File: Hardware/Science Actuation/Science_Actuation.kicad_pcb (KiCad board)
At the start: 2 copper layers, 111 parts, among them J4 RJ45_LED_Shielded, Q1 BSS138, Q2 BSS138, Q3 BSS138, Q4 AO3401A, Q5 AO3401A, SW1 SW_Push, SW10 SW_SPDT, SW2 SW_Push, SW3 SW_Push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

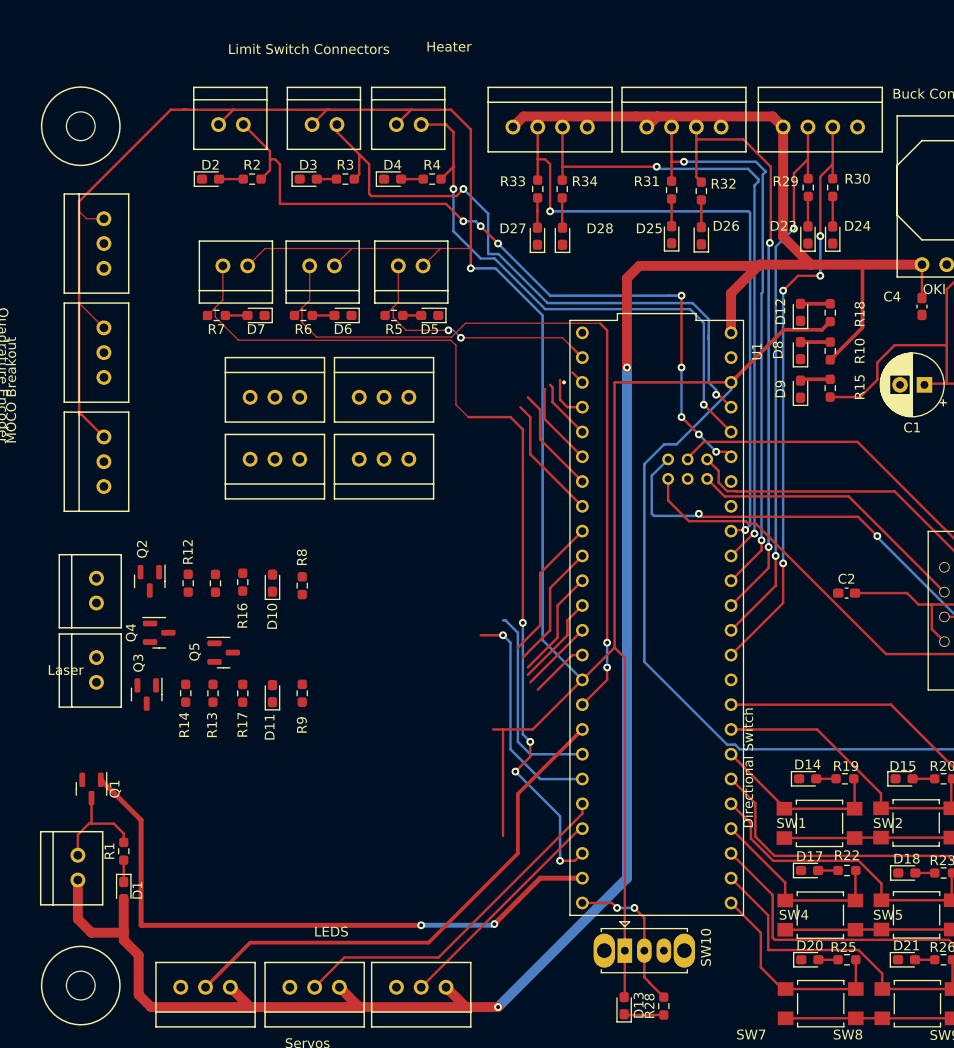
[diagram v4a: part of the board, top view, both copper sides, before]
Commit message: Tried  Cleaning Up Board
Changed layout, added fourth MOCO Breakout
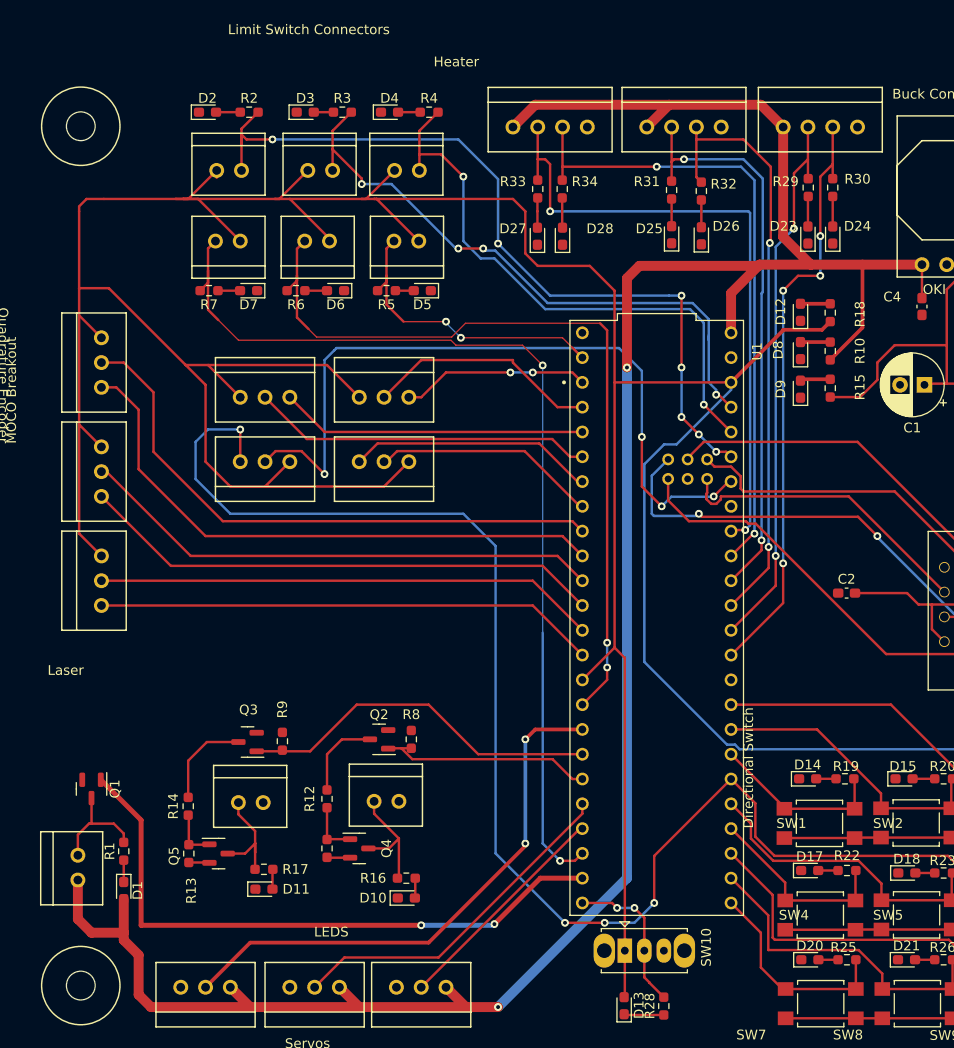
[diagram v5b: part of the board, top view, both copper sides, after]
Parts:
- moved D10 35.1 mm to (49.5, 95.2), turned to 0 degrees
- moved Conn12 35.0 mm to (46.2, 85.3), turned to 0 degrees
- moved R16 34.7 mm to (49.5, 93.2), turned to 180 degrees
- moved Conn16 34.5 mm to (18.3, 65.3)
- moved Q4 30.1 mm to (44.7, 90.2)
- moved R11 29.5 mm to (41.4, 90.2)
- moved Q2 28.5 mm to (46.7, 79.0), turned to 180 degrees
- moved R12 26.3 mm to (41.4, 85.1), turned to 90 degrees
- moved Q5 20.6 mm to (30.3, 90.7)
- moved D11 20.1 mm to (34.9, 94.3), turned to 0 degrees
- moved R8 19.3 mm to (50.0, 79.0), turned to 90 degrees
- moved Conn13 19.1 mm to (32.3, 85.5), turned to 0 degrees
- moved R17 18.2 mm to (34.9, 92.3), turned to 180 degrees
- moved R13 16.6 mm to (27.2, 90.7), turned to 90 degrees
- moved Conn15 12.2 mm to (18.3, 54.1)
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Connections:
- U1 pad 10: Heater_On2 -> Heater_Temp2
- U1 pad 11: Heater_Temp3 -> Heater_On3
- U1 pad 12: Heater_On3 -> Heater_Temp3
- U1 pad 20: MOCO3_FWD -> MOCO4_FWD
- U1 pad 38: MOCO3_RVS -> MOCO4_RVS
- U1 pad 7: Heater_Temp -> Heater_On
- U1 pad 8: Heater_On -> Heater_Temp
- U1 pad 9: Heater_Temp2 -> Heater_On2
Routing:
- net MOCO4_RVS: track 0.00 -> 112.8 mm, vias 0 -> 4
- net MOCO4_FWD: track 0.00 -> 76.1 mm, vias 0 -> 4
- net Heater_On: track 12.9 -> 60.0 mm
- net Heater_On3: track 6.04 -> 51.4 mm
- net Heater_Temp: track 14.7 -> 60.0 mm
- net Heater_On2: track 9.43 -> 53.9 mm
- net Heater_Temp3: track 7.54 -> 51.4 mm
- net Heater_Temp2: track 11.2 -> 53.9 mm
- net +3V3: track 482.4 -> 510.1 mm, vias 2 -> 1
- net MOCO2_FWD: track 8.62 -> 35.0 mm
- net MOCO2_RVS: track 6.21 -> 31.4 mm
- net MOCO3_FWD: track 4.63 -> 24.1 mm
- net MOCO3_RVS: track 1.44 -> 19.3 mm, vias 0 -> 2
- net Pump2: track 20.4 -> 37.6 mm
- net MOCO1_RVS: track 11.0 -> 25.3 mm
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
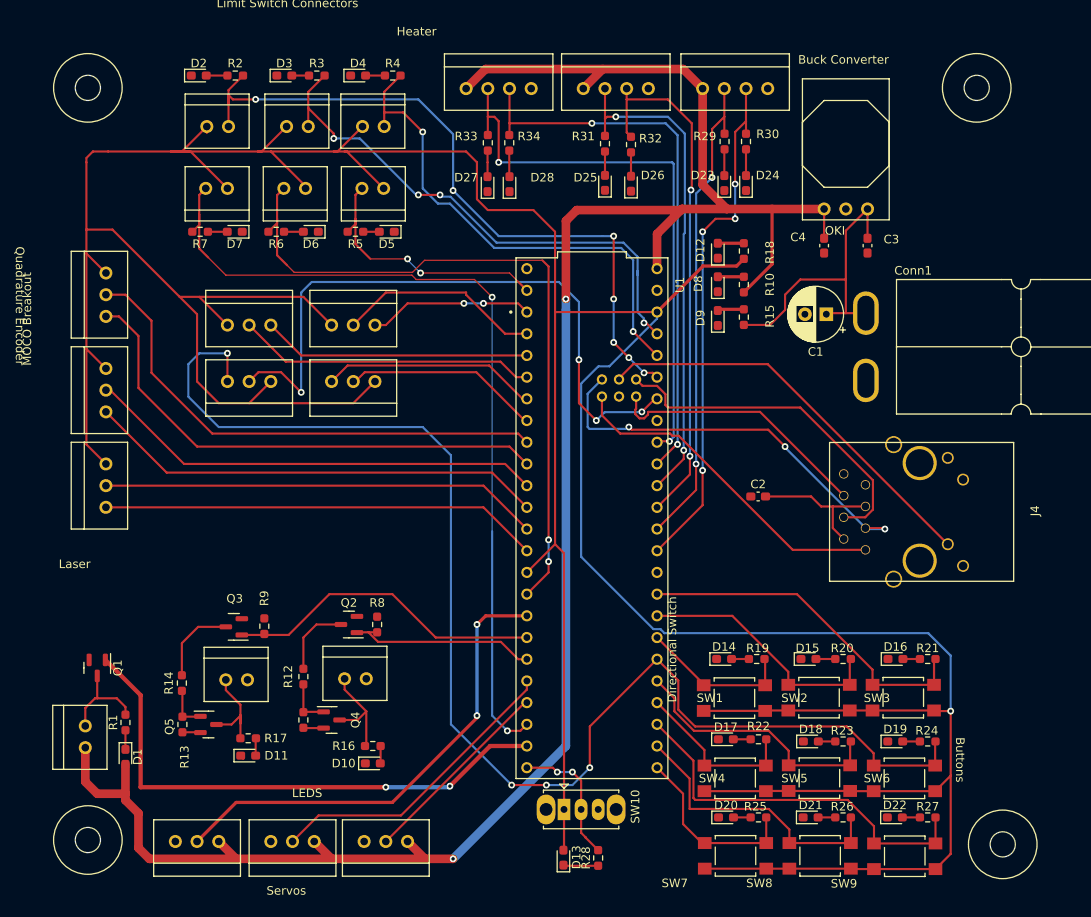
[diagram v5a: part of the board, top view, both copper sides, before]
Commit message: Added edge cuts
Added edge cuts
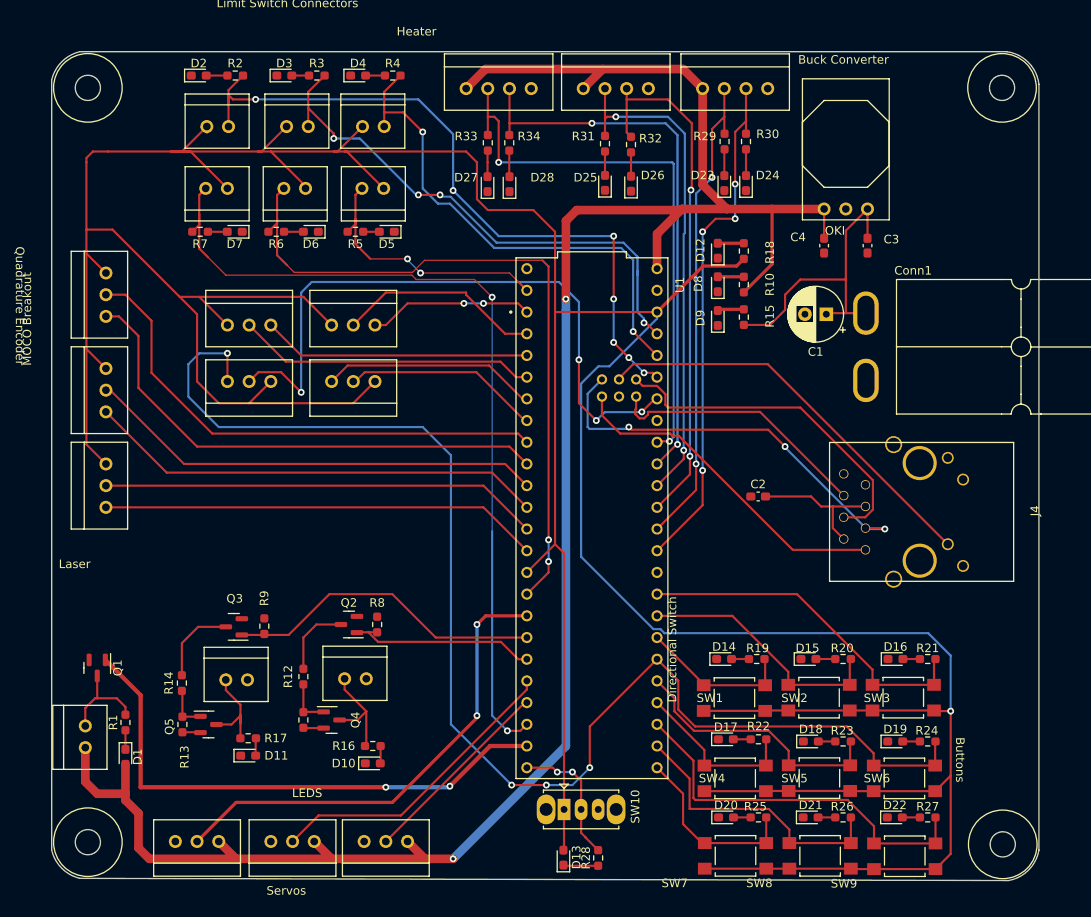
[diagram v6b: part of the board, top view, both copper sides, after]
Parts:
- moved H2 2.97 mm to (119.2, 20.2)
- moved H4 0.25 mm to (20.2, 100.5)
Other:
- board outline added: 115.6 x 97 mm
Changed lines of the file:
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@@
   )
   (footprint "MRDT_Drill_Holes:4_40_Hole_Corner" (layer "F.Cu")
-    (at 20.1817 100.2143 180)
+    (at 20.1817 100.4683 180)
     (property "Sheetfile" "Science_Actuation.kicad_sch")
     (property "Sheetname" "")
@@
   )
   (footprint "MRDT_Drill_Holes:4_40_Hole_Corner" (layer "F.Cu")
-    (at 116.2163 20.1817)
+    (at 119.18188 20.1817)
     (property "Sheetfile" "Science_Actuation.kicad_sch")
     (property "Sheetname" "")
@@
     )
   )
+  (gr_arc (start 11.938 15.24) (mid 13.119331 13.119331) (end 15.24 11.938)
+    (stroke (width 0.1) (type default)) (layer "Edge.Cuts"))
+  (gr_arc (start 123.729276 11.941795) (mid 126.275463 13.192815) (end 127.507999 15.748)
+    (stroke (width 0.1) (type default)) (layer "Edge.Cuts"))
+  (gr_line (start 123.952 108.965999) (end 15.24 108.712)
+    (stroke (width 0.1) (type default)) (layer "Edge.Cuts"))
+  (gr_line (start 15.24 11.938) (end 123.729276 11.941795)
+    (stroke (width 0.1) (type default)) (layer "Edge.Cuts"))
+  (gr_arc (start 127.507999 105.41) (mid 126.290464 107.748464) (end 123.952 108.965999)
+    (stroke (width 0.1) (type default)) (layer "Edge.Cuts"))
+  (gr_arc (start 15.24 108.712) (mid 13.119331 107.530669) (end 11.938 105.41)
+    (stroke (width 0.1) (type default)) (layer "Edge.Cuts"))
+  (gr_line (start 127.507999 15.748) (end 127.507999 105.41)
+    (stroke (width 0.1) (type default)) (layer "Edge.Cuts"))
+  (gr_line (start 11.938 105.41) (end 11.938 15.24)
+    (stroke (width 0.1) (type default)) (layer "Edge.Cuts"))
   (gr_text "LEDS" (at 40.066 99.314) (layer "F.SilkS")
     (effects (font (size 1 1) (thickness 0.15)) (justify left bottom))

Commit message: Temporary update
Passing on the torch
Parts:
- moved D19 4.33 mm to (111.3, 88.4)
- moved R24 4.33 mm to (115.1, 88.4)
- moved D18 4.31 mm to (101.1, 88.4)
- moved R23 4.31 mm to (104.9, 88.4)
- moved D20 4.18 mm to (89.8, 97.5)
- moved R25 4.18 mm to (93.6, 97.5)
- moved D14 4.07 mm to (90.4, 79.0)
- moved D15 4.07 mm to (100.3, 79.0)
- moved D16 4.07 mm to (110.5, 79.0)
- moved R19 4.07 mm to (94.3, 79.0)
- moved R20 4.07 mm to (104.4, 79.0)
- moved SW2 4.07 mm to (101.6, 83.5)
- moved SW5 4.07 mm to (101.6, 92.9)
- moved SW6 4.07 mm to (111.5, 92.9)
- moved D17 4.07 mm to (90.6, 88.4)
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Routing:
- net +3V3: track 510.1 -> 553.0 mm
- net SW6: track 43.4 -> 80.2 mm, vias 0 -> 2
- net T-: track 48.7 -> 33.4 mm, vias 3 -> 2
- net SW5: track 31.4 -> 35.9 mm
- net SW9: track 45.2 -> 49.4 mm, vias 0 -> 2
- net SW4: track 20.0 -> 23.4 mm
- net LED: track 48.0 -> 50.9 mm
- net T+: track 39.6 -> 42.4 mm
- net R+: track 40.6 -> 43.4 mm
- net R-: track 31.3 -> 33.8 mm
- net SW7: track 21.5 -> 23.2 mm
- net SW8: track 33.4 -> 34.8 mm
- net +12V: track 42.4 -> 43.6 mm
- net SW1: track 18.2 -> 17.4 mm
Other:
- board text added: "Anderson"
- board text added: "Ethernet"
- board text added: "Oki"
- board text added: "Pumps"
- board text added: "Teensy"
- board text removed: "Buck Converter"

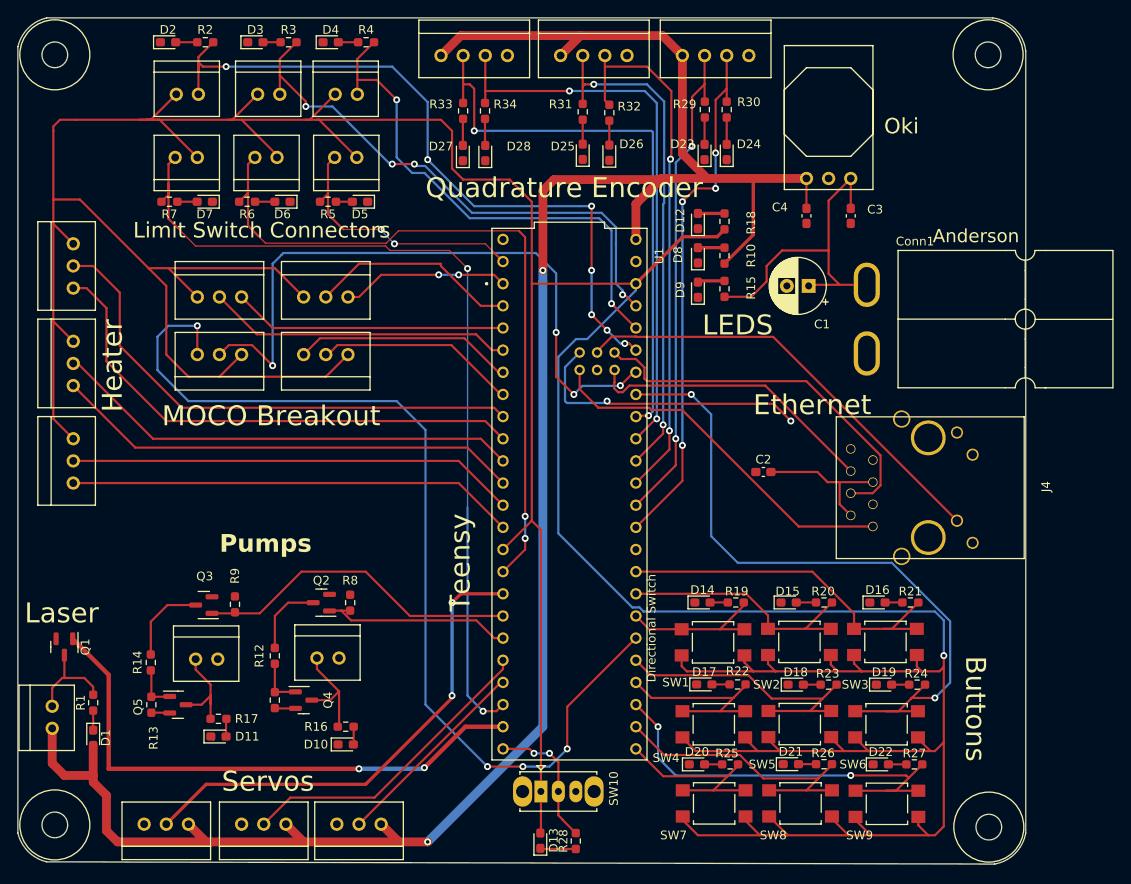
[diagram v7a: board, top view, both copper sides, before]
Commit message: Fixed mounting hole locations, did ethernet t+/-, still need ground plane
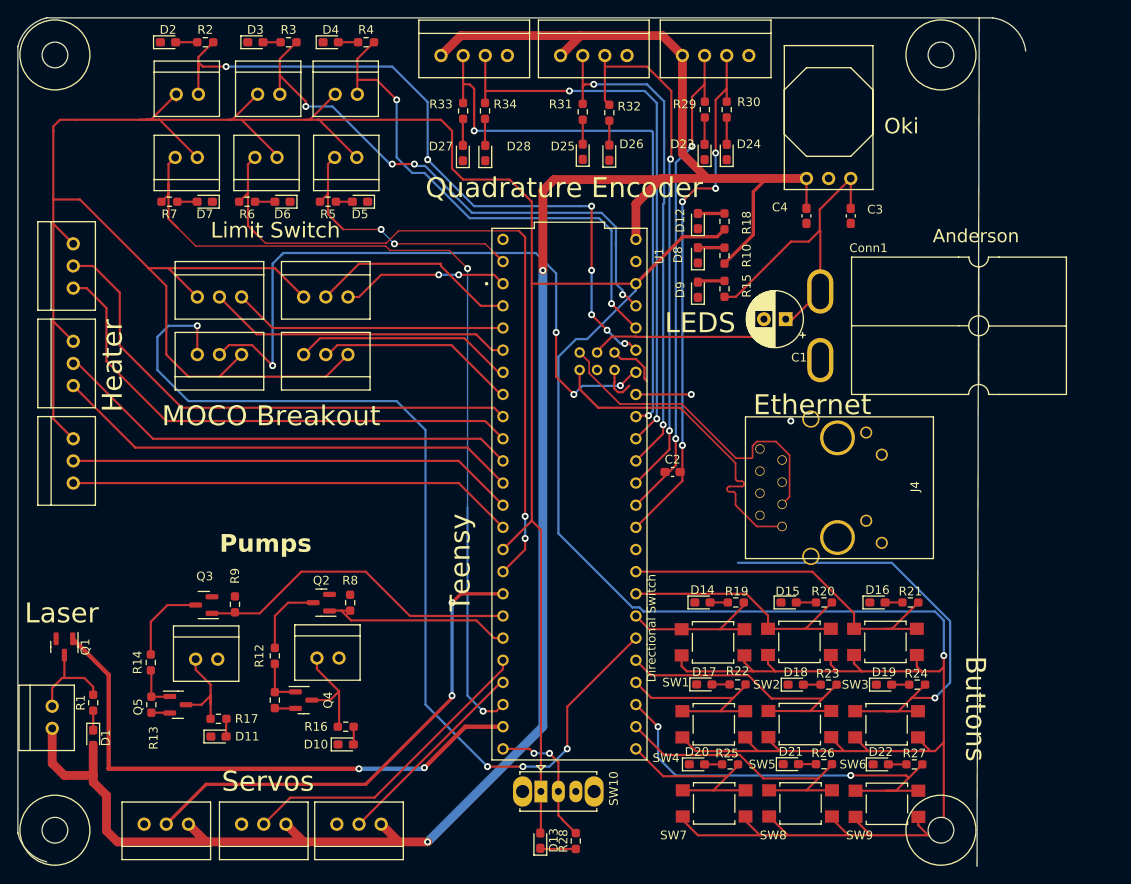
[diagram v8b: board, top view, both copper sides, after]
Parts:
- moved C2 10.4 mm to (87.0, 64.0)
- moved J4 10.4 mm to (118.9, 65.7)
- moved H3 5.50 mm to (113.8, 101.1)
- moved H2 5.41 mm to (113.8, 20.2)
- moved Conn1 5.39 mm to (103.6, 51.7)
- moved C1 4.63 mm to (100.0, 46.5)
- moved H4 0.61 mm to (20.2, 101.1)
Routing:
- net R+: track 43.4 -> 5.83 mm
- net LED: track 50.9 -> 21.0 mm
- net R-: track 33.8 -> 4.38 mm
- net SW6: track 80.2 -> 58.7 mm
- net Net-(C2-Pad2): track 16.5 -> 0.00 mm
- net T-: track 33.4 -> 38.0 mm, vias 2 -> 1
- net T+: track 42.4 -> 37.9 mm
- net +5V: track 247.6 -> 248.3 mm
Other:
- board size 115.6 x 97 mm -> 115.6 x 97.3 mm
- board text added: "Limit Switch"
- board text removed: "Limit Switch Connectors"
